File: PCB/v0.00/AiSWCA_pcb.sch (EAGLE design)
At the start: 24 parts, among them IC1 LM1117IMPX-3.3, IC2 AD8400R, T1 BC847

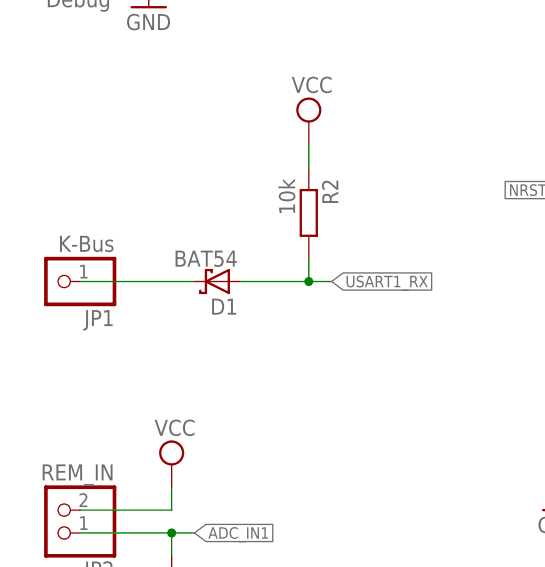
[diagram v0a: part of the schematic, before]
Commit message: Replaced previous Schottky diode with one in SOD323 package.
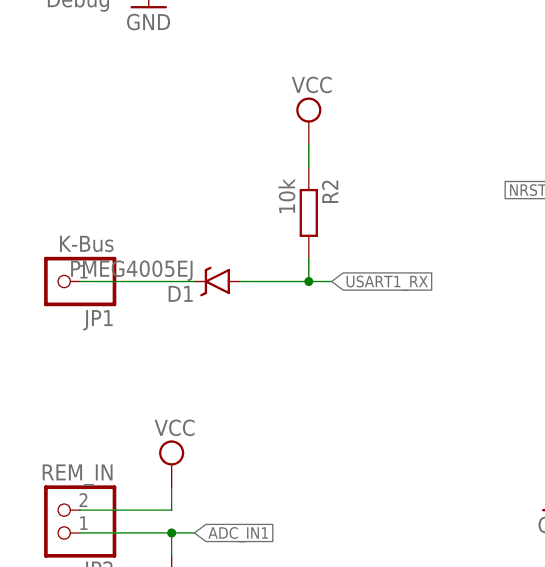
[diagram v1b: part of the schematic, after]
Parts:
- D1: value BAT54 -> PMEG4005EJ; device diode:BAT54 -> SparkFun-DiscreteSemi:DIODE-SCHOTTKY-PMEG4005EJ
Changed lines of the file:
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@@
 <layer number="54" name="bGND_GNDA" color="7" fill="1" visible="no" active="no"/>
 <layer number="56" name="wert" color="7" fill="1" visible="no" active="no"/>
+<layer number="57" name="tCAD" color="7" fill="1" visible="no" active="no"/>
+<layer number="59" name="tCarbon" color="7" fill="1" visible="no" active="no"/>
+<layer number="60" name="bCarbon" color="7" fill="1" visible="no" active="no"/>
+<layer number="90" name="Modules" color="5" fill="1" visible="yes" active="yes"/>
 <layer number="91" name="Nets" color="2" fill="1" visible="yes" active="yes"/>
 <layer number="92" name="Busses" color="1" fill="1" visible="yes" active="yes"/>
@@
 <layer number="109" name="fp9" color="7" fill="1" visible="yes" active="yes"/>
 <layer number="110" name="fp0" color="7" fill="1" visible="yes" active="yes"/>
+<layer number="111" name="LPC17xx" color="7" fill="1" visible="yes" active="yes"/>
+<layer number="112" name="tSilk" color="7" fill="1" visible="yes" active="yes"/>
+<layer number="113" name="IDFDebug" color="7" fill="1" visible="yes" active="yes"/>
 <layer number="116" name="Patch_BOT" color="7" fill="1" visible="yes" active="yes"/>
+<layer number="118" name="Rect_Pads" color="7" fill="1" visible="yes" active="yes"/>
 <layer number="121" name="tTestdril" color="7" fill="1" visible="yes" active="yes"/>
 <layer number="122" name="bTestdril" color="7" fill="1" visible="yes" active="yes"/>
 <layer number="123" name="tTestmark" color="7" fill="1" visible="yes" active="yes"/>
 <layer number="124" name="bTestmark" color="7" fill="1" visible="yes" active="yes"/>
+<layer number="125" name="_tNames" color="7" fill="1" visible="yes" active="yes"/>
+<layer number="126" name="_bNames" color="7" fill="1" visible="yes" active="yes"/>
+<layer number="127" name="_tValues" color="7" fill="1" visible="yes" active="yes"/>
+<layer number="128" name="_bValues" color="7" fill="1" visible="yes" active="yes"/>
+<layer number="129" name="Mask" color="7" fill="1" visible="yes" active="yes"/>
 <layer number="131" name="tAdjust" color="7" fill="1" visible="yes" active="yes"/>
 <layer number="132" name="bAdjust" color="7" fill="1" visible="yes" active="yes"/>
+<layer number="144" name="Drill_legend" color="7" fill="1" visible="yes" active="yes"/>
+<layer number="150" name="Notes" color="7" fill="1" visible="yes" active="yes"/>
 <layer number="151" name="HeatSink" color="7" fill="1" visible="yes" active="yes"/>
+<layer number="152" name="_bDocu" color="7" fill="1" visible="yes" active="yes"/>
+<layer number="153" name="FabDoc1" color="7" fill="1" visible="yes" active="yes"/>
+<layer number="154" name="FabDoc2" color="7" fill="1" visible="yes" active="yes"/>
+<layer number="155" name="FabDoc3" color="7" fill="1" visible="yes" active="yes"/>
+<layer number="199" name="Contour" color="7" fill="1" visible="yes" active="yes"/>
 <layer number="200" name="200bmp" color="1" fill="10" visible="no" active="no"/>
 <layer number="201" name="201bmp" color="7" fill="1" visible="yes" active="yes"/>
@@
 <layer number="230" name="230bmp" color="7" fill="1" visible="yes" active="yes"/>
 <layer number="231" name="231bmp" color="7" fill="1" visible="yes" active="yes"/>
+<layer number="248" name="Housing" color="7" fill="1" visible="yes" active="yes"/>
+<layer number="249" name="Edge" color="7" fill="1" visible="yes" active="yes"/>
 <layer number="250" name="Descript" color="3" fill="1" visible="no" active="no"/>
 <layer number="251" name="SMDround" color="12" fill="11" visible="no" active="no"/>
 <layer number="254" name="OrgLBR" color="7" fill="1" visible="yes" active="yes"/>
+<layer number="255" name="routoute" color="7" fill="1" visible="yes" active="yes"/>
 </layers>
 <schematic xreflabel="%F%N/%S.%C%R" xrefpart="/%S.%C%R">
@@
 <part name="SV2" library="con-lstb" deviceset="MA03-1" device="" value="Debug"/>
 <part name="GND1" library="supply1" deviceset="GND" device=""/>
-<part name="D1" library="diode" deviceset="BAT54" device=""/>
+<part name="D1" library="SparkFun-DiscreteSemi" deviceset="DIODE-SCHOTTKY" device="-PMEG4005EJ" value="PMEG4005EJ"/>
 <part name="SUPPLY2" library="supply2" deviceset="VCC" device=""/>
 <part name="R2" library="rcl" deviceset="R-EU_" device="R0805" value="10k"/>

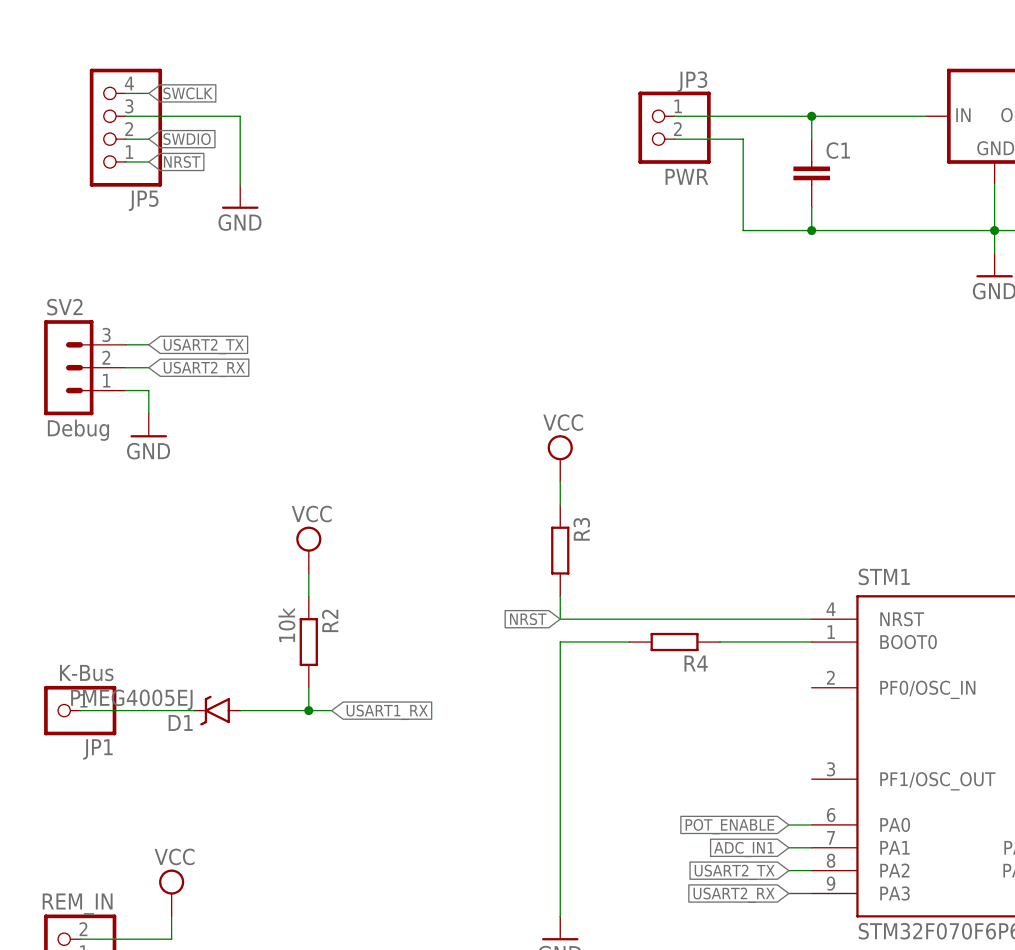
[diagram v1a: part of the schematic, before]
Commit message: Added diode (SOD323 package) on power section
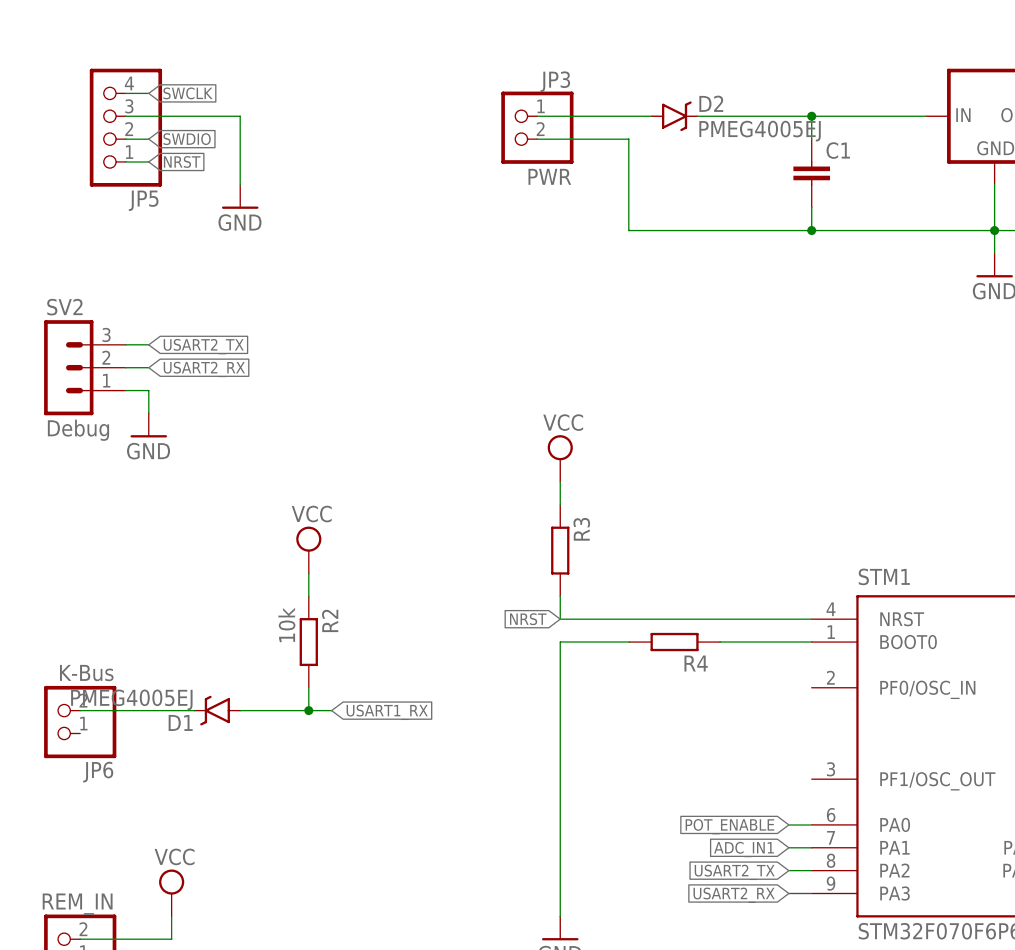
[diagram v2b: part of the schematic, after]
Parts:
- removed JP1: K-Bus, pinhead:PINHD-1X1
- added D2: PMEG4005EJ, SparkFun-DiscreteSemi:DIODE-SCHOTTKY-PMEG4005EJ
- added JP6: K-Bus, pinhead:PINHD-1X2/90
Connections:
- new net N$4: D2.A, JP3.1
- net N$1: now also D2.C; no longer JP3.1
- net N$3: now also JP6.2; no longer JP1.1
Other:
- moved on the sheet: JP3
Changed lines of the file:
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@@
 <part name="SUPPLY6" library="supply2" deviceset="VCC" device=""/>
 <part name="JP2" library="pinhead" deviceset="PINHD-1X2" device="/90" value="REM_IN"/>
-<part name="JP1" library="pinhead" deviceset="PINHD-1X1" device="" value="K-Bus"/>
 <part name="JP4" library="pinhead" deviceset="PINHD-1X2" device="/90" value="Remote"/>
 <part name="JP5" library="pinhead" deviceset="PINHD-1X4" device="/90"/>
+<part name="D2" library="SparkFun-DiscreteSemi" deviceset="DIODE-SCHOTTKY" device="-PMEG4005EJ" value="PMEG4005EJ"/>
+<part name="JP6" library="pinhead" deviceset="PINHD-1X2" device="/90" value="K-Bus"/>
 </parts>
 <sheets>
@@
 <instance part="GND7" gate="1" x="152.4" y="40.64"/>
 <instance part="GND3" gate="1" x="-15.24" y="53.34"/>
-<instance part="JP3" gate="G$1" x="30.48" y="60.96" rot="MR0"/>
+<instance part="JP3" gate="G$1" x="15.24" y="60.96" rot="MR0"/>
 <instance part="IC1" gate="G$1" x="68.58" y="63.5"/>
 <instance part="C1" gate="G$1" x="48.26" y="58.42"/>
@@
 <instance part="SUPPLY6" gate="G$1" x="104.14" y="25.4"/>
 <instance part="JP2" gate="G$1" x="-35.56" y="-27.94" rot="R180"/>
-<instance part="JP1" gate="G$1" x="-35.56" y="-2.54" rot="R180"/>
 <instance part="JP4" gate="G$1" x="137.16" y="-12.7" rot="R180"/>
 <instance part="JP5" gate="A" x="-30.48" y="63.5" rot="R180"/>
+<instance part="D2" gate="G$1" x="33.02" y="63.5"/>
+<instance part="JP6" gate="G$1" x="-35.56" y="-2.54" rot="R180"/>
 </instances>
 <busses>
@@
 <wire x1="86.36" y1="50.8" x2="86.36" y2="53.34" width="0.1524" layer="91"/>
 <pinref part="GND5" gate="1" pin="GND"/>
+<wire x1="48.26" y1="50.8" x2="27.94" y2="50.8" width="0.1524" layer="91"/>
+<wire x1="27.94" y1="50.8" x2="27.94" y2="60.96" width="0.1524" layer="91"/>
+<junction x="48.26" y="50.8"/>
 <pinref part="JP3" gate="G$1" pin="2"/>
-<wire x1="33.02" y1="60.96" x2="40.64" y2="60.96" width="0.1524" layer="91"/>
-<wire x1="40.64" y1="60.96" x2="40.64" y2="50.8" width="0.1524" layer="91"/>
-<wire x1="40.64" y1="50.8" x2="48.26" y2="50.8" width="0.1524" layer="91"/>
-<junction x="48.26" y="50.8"/>
+<wire x1="27.94" y1="60.96" x2="17.78" y2="60.96" width="0.1524" layer="91"/>
 </segment>
 <segment>
@@
 <pinref part="C1" gate="G$1" pin="1"/>
 <wire x1="48.26" y1="60.96" x2="48.26" y2="63.5" width="0.1524" layer="91"/>
+<pinref part="D2" gate="G$1" pin="C"/>
+<wire x1="35.56" y1="63.5" x2="48.26" y2="63.5" width="0.1524" layer="91"/>
 <junction x="48.26" y="63.5"/>
-<pinref part="JP3" gate="G$1" pin="1"/>
-<wire x1="33.02" y1="63.5" x2="48.26" y2="63.5" width="0.1524" layer="91"/>
 </segment>
 </net>
@@
 <pinref part="D1" gate="G$1" pin="C"/>
 <wire x1="-33.02" y1="-2.54" x2="-20.32" y2="-2.54" width="0.1524" layer="91"/>
-<pinref part="JP1" gate="G$1" pin="1"/>
+<pinref part="JP6" gate="G$1" pin="2"/>
 </segment>
 </net>
@@
 </segment>
 </net>
+<net name="N$4" class="0">
+<segment>
+<pinref part="JP3" gate="G$1" pin="1"/>
+<pinref part="D2" gate="G$1" pin="A"/>
+<wire x1="17.78" y1="63.5" x2="30.48" y2="63.5" width="0.1524" layer="91"/>
+</segment>
+</net>

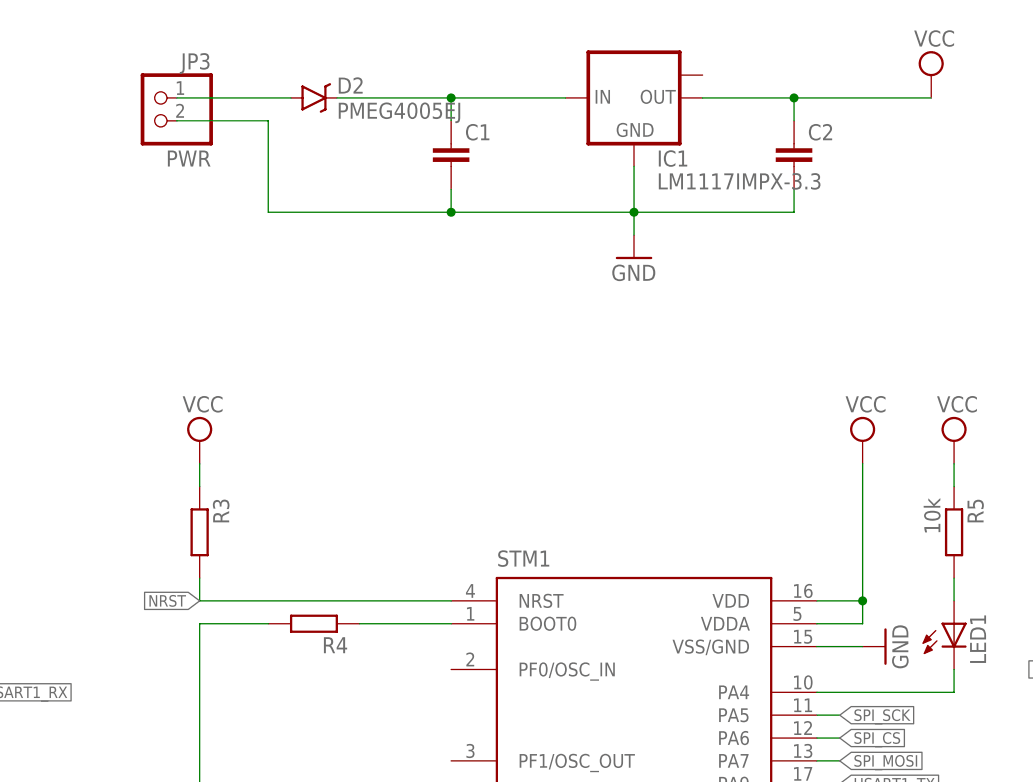
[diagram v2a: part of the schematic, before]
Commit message: Added values to some of elements on schematics.
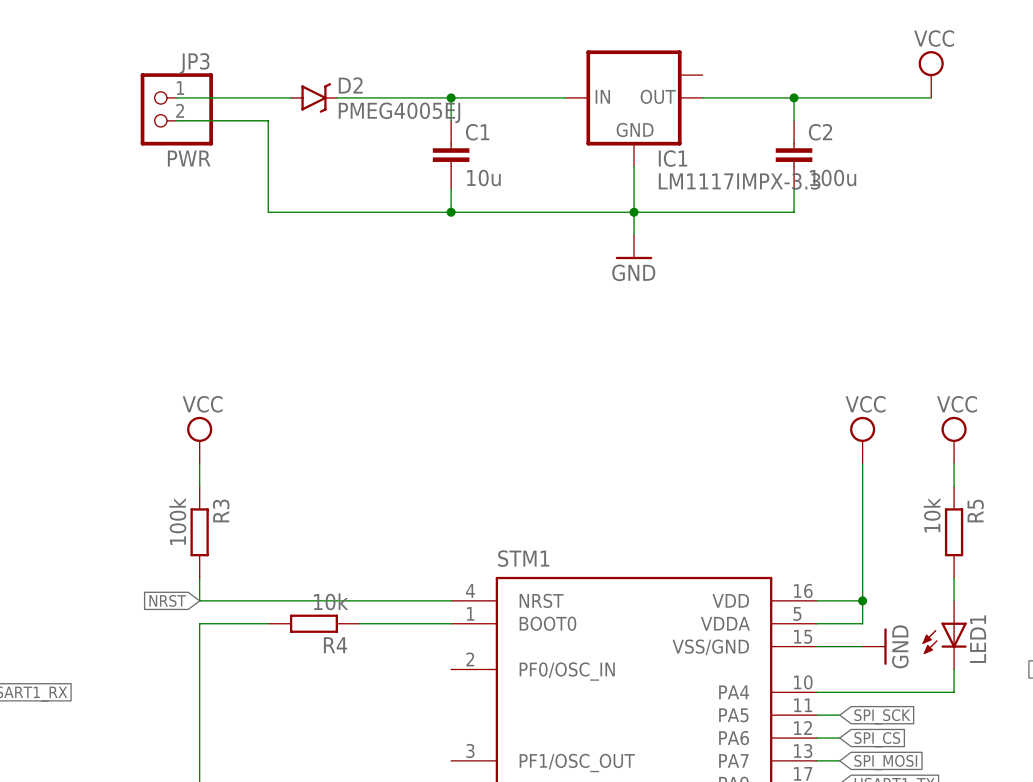
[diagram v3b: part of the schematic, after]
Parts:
- C1: value (none) -> 10u
- C2: value (none) -> 100u
- R3: value (none) -> 100k
- R4: value (none) -> 10k
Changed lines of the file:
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@@
 <parts>
 <part name="STM1" library="stm32f030f4" deviceset="STM32F030F4P6" device="V1" value="STM32F070F6P6"/>
-<part name="R4" library="rcl" deviceset="R-EU_" device="R0805"/>
-<part name="R3" library="rcl" deviceset="R-EU_" device="R0805"/>
+<part name="R4" library="rcl" deviceset="R-EU_" device="R0805" value="10k"/>
+<part name="R3" library="rcl" deviceset="R-EU_" device="R0805" value="100k"/>
 <part name="GND4" library="supply1" deviceset="GND" device=""/>
 <part name="GND6" library="supply1" deviceset="GND" device=""/>
@@
 <part name="JP3" library="pinhead" deviceset="PINHD-1X2" device="/90" value="PWR"/>
 <part name="IC1" library="lm1117" deviceset="LM1117IMPX-*" device="" technology="3.3"/>
-<part name="C1" library="rcl" deviceset="C-EU" device="C0805"/>
-<part name="C2" library="rcl" deviceset="C-EU" device="C0805"/>
+<part name="C1" library="rcl" deviceset="C-EU" device="C0805" value="10u"/>
+<part name="C2" library="rcl" deviceset="C-EU" device="C0805" value="100u"/>
 <part name="GND5" library="supply1" deviceset="GND" device=""/>
 <part name="SUPPLY5" library="supply2" deviceset="VCC" device=""/>
